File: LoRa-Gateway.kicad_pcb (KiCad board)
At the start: 2 copper layers, 83 x 29 mm, 47 parts, among them IC1 LT8609MSE, J1 Conn_Coaxial, J2 Conn_01x06, J3 Conn_01x04, J4 Conn_01x02, J5 Conn_01x01, J6 Conn_01x01, J7 Conn_01x01, J8 Conn_Coaxial, U1 RFM95W-868S2, U2 ESP-12E

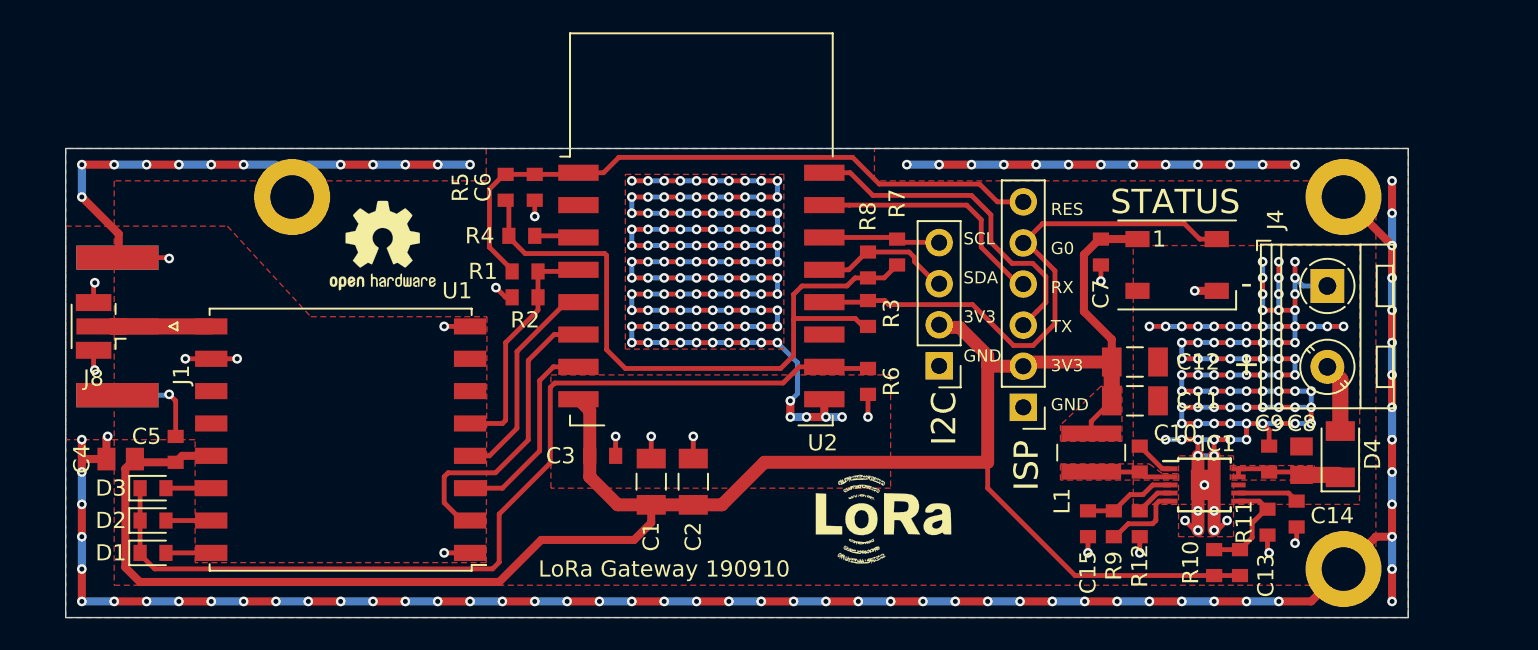
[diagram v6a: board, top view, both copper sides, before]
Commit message: Added Power flags, adden more vias around antenna connector, ERC, DRC
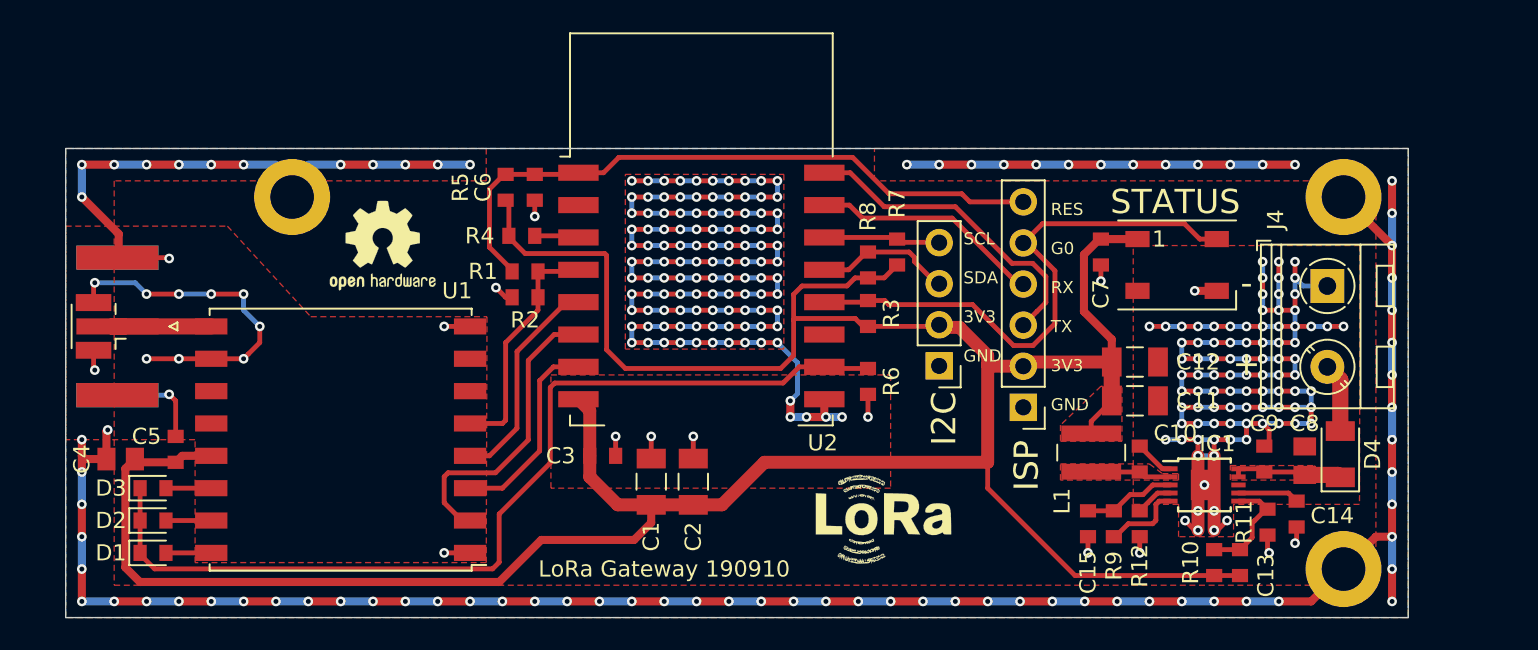
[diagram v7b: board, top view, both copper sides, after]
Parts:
- LED1: footprint LED_SMD:LED_WS2812B_PLCC4_5.0x5.0mm_P3.2mm -> kicad-footprints-master:LED_WS2812B_PLCC4_5.0x5.0mm_P3.2mm
- moved C9 0.30 mm to (190.1, 76.2)
- moved C8 0.20 mm to (192.6, 76.3)
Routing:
- net GND: track 435.6 -> 453.1 mm, vias 309 -> 315
- net +3V3: track 175.7 -> 180.2 mm
- net /TX: track 20.9 -> 19.9 mm
- net /RX: track 15.3 -> 14.3 mm
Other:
- rule trace_min: 0.2 -> 0.1
